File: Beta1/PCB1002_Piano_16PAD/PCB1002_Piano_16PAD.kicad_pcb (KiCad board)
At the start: 2 copper layers, 194 x 64 mm, 47 parts, among them U1 MPR121OTS, U2 MPR121OTS, U3 MPR121OTS

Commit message: Placement Done.
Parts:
- removed +3.3VA0, +3.3VB0, +3.3VC0, GNDA0, GNDB0, GNDC0, IRQA0, IRQB0, IRQC0, SCLA0, SCLB0, SCLC0, SDAA0, SDAB0, SDAC0: CONN_01X01, Liberry:single_0.1
- removed the REF** at (20.3, -2.54)
- removed the REF** at (8.64, -39.6)
- removed U2, U3: MPR121OTS, Liberry:MPR121OTS
- added A0: CONN_01X01, Liberry:TH_0.1_1x2_Jumper, F.Cu at (6.35, -22.9)
- added A1: CONN_01X01, Liberry:TH_0.1_1x2_Jumper, F.Cu at (6.35, -20.3)
- added A2: CONN_01X01, Liberry:TH_0.1_1x2_Jumper, F.Cu at (6.35, -17.8)
- added A3: CONN_01X01, Liberry:TH_0.1_1x2_Jumper, F.Cu at (6.35, -15.2)
- added A4: CONN_01X01, Liberry:TH_0.1_1x2_Jumper, F.Cu at (6.35, -12.7)
- added A5: CONN_01X01, Liberry:TH_0.1_1x2_Jumper, F.Cu at (6.35, -10.2)
- added C1: CC0603KRX7R9BB104, Capacitors_SMD:C_0603, B.Cu at (12.7, -50.8)
- added C101: CC0603KRX7R9BB104, Capacitors_SMD:C_0603, B.Cu at (12.7, -22.9)
- added C102: 0.1uf, Capacitors_SMD:C_0603, B.Cu at (12.7, -39.4)
- added C2: 0.1uf, Capacitors_SMD:C_0603, B.Cu at (12.7, -61.0)
- added C201: CC0603KRX7R9BB104, Capacitors_SMD:C_0603, B.Cu at (12.7, -3.29)
- added C202: 0.1uf, Capacitors_SMD:C_0603, B.Cu at (12.7, -15.2)
- added P0: CONN_01X01, Liberry:TESTPAD, B.Cu at (33.8, -52.1)
- added P1: CONN_01X01, Liberry:TESTPAD, B.Cu at (53.8, -52.1)
- added P10: CONN_01X01, Liberry:TESTPAD, B.Cu at (17.8, -48.3)
- added P100: CONN_01X01, Liberry:TESTPAD, B.Cu at (33.8, -32.1)
- added P101: CONN_01X01, Liberry:TESTPAD, B.Cu at (53.8, -32.1)
- added P102: CONN_01X01, Liberry:TESTPAD, B.Cu at (73.8, -32.1)
- added P103: CONN_01X01, Liberry:TESTPAD, B.Cu at (93.8, -32.1)
- added P104: CONN_01X01, Liberry:TESTPAD, B.Cu at (113.8, -32.1)
- added P105: CONN_01X01, Liberry:TESTPAD, B.Cu at (133.8, -32.1)
- added P106: CONN_01X01, Liberry:TESTPAD, B.Cu at (153.8, -32.1)
- added P107: CONN_01X01, Liberry:TESTPAD, B.Cu at (173.3, -32.1)
- added P108: CONN_01X01, Liberry:TESTPAD, B.Cu at (22.9, -22.9)
- added P109: CONN_01X01, Liberry:TESTPAD, B.Cu at (20.3, -22.9)
- added P11: CONN_01X01, Liberry:TESTPAD, B.Cu at (15.2, -48.3)
- added P110: CONN_01X01, Liberry:TESTPAD, B.Cu at (17.8, -22.9)
- added P111: CONN_01X01, Liberry:TESTPAD, B.Cu at (15.2, -22.9)
- added P2: CONN_01X01, Liberry:TESTPAD, B.Cu at (73.8, -52.1)
- added P200: CONN_01X01, Liberry:TESTPAD, B.Cu at (35.2, -4.88)
- added P201: CONN_01X01, Liberry:TESTPAD, B.Cu at (46.6, -16.1)
- added P202: CONN_01X01, Liberry:TESTPAD, B.Cu at (58.0, -4.88)
- added P203: CONN_01X01, Liberry:TESTPAD, B.Cu at (69.5, -16.1)
- added P204: CONN_01X01, Liberry:TESTPAD, B.Cu at (80.9, -4.88)
- added P205: CONN_01X01, Liberry:TESTPAD, B.Cu at (103.8, -4.88)
- added P206: CONN_01X01, Liberry:TESTPAD, B.Cu at (115.2, -16.1)
- added P207: CONN_01X01, Liberry:TESTPAD, B.Cu at (126.6, -4.88)
- added P208: CONN_01X01, Liberry:TESTPAD, B.Cu at (138.0, -16.1)
- added P209: CONN_01X01, Liberry:TESTPAD, B.Cu at (149.5, -4.88)
- added P210: CONN_01X01, Liberry:TESTPAD, B.Cu at (160.9, -16.1)
- added P211: CONN_01X01, Liberry:TESTPAD, B.Cu at (172.3, -4.88)
- added P3: CONN_01X01, Liberry:TESTPAD, B.Cu at (93.8, -52.1)
- added P4: CONN_01X01, Liberry:TESTPAD, B.Cu at (113.8, -52.1)
- added P5: CONN_01X01, Liberry:TESTPAD, B.Cu at (133.8, -52.1)
- added P6: CONN_01X01, Liberry:TESTPAD, B.Cu at (153.8, -52.1)
- added P7: CONN_01X01, Liberry:TESTPAD, B.Cu at (173.8, -52.1)
- added P8: CONN_01X01, Liberry:TESTPAD, B.Cu at (22.9, -48.3)
- added P9: CONN_01X01, Liberry:TESTPAD, B.Cu at (20.3, -48.3)
- added R1: 75K, Resistors_SMD:R_0603, B.Cu at (17.8, -61.0)
- added R101: 75K, Resistors_SMD:R_0603, B.Cu at (17.8, -39.4)
- added R102: 100K, Resistors_SMD:R_0603, B.Cu at (15.2, -39.4)
- added R2: 100K, Resistors_SMD:R_0603, B.Cu at (15.2, -61.0)
- added R201: 75K, Resistors_SMD:R_0603, B.Cu at (17.8, -15.2)
- added R202: 100K, Resistors_SMD:R_0603, B.Cu at (15.2, -15.2)
- added R301: 10K, Resistors_SMD:R_0603, B.Cu at (11.4, -33.0)
- added R302: 10K, Resistors_SMD:R_0603, B.Cu at (11.4, -30.5)
- added R303: 10K, Resistors_SMD:R_0603, B.Cu at (11.4, -35.6)
- added REF**: Fiducial_1mm_Dia_2.54mm_Outer_CopperBottom, Fiducials:Fiducial_1mm_Dia_2.54mm_Outer_CopperBottom, F.Cu at (7.62, -55.9)
- added U100: MPR121QR2, Liberry:QFN-20-1EP_3x3mm_Pitch0.40mm, B.Cu at (20.3, -29.3)
- added U200: MPR121QR2, Liberry:QFN-20-1EP_3x3mm_Pitch0.40mm, B.Cu at (20.3, -9.36)
- +3.3V0, GND0, IRQ0, SCL0, SDA0: footprint Liberry:single_0.1 -> Liberry:TH_0.1_1x2_Jumper
- U1: value MPR121OTS -> MPR121QR2; footprint Liberry:MPR121OTS -> Liberry:QFN-20-1EP_3x3mm_Pitch0.40mm; moved to B.Cu
- moved U1 24.2 mm to (20.3, -54.7)
- moved +3.3V0 20.4 mm to (6.35, -35.6)
- moved GND0 20.4 mm to (6.35, -25.4)
- moved IRQ0 20.4 mm to (6.35, -33.0)
- moved SCL0 20.4 mm to (6.35, -27.9)
- moved SDA0 20.4 mm to (6.35, -30.5)
- moved REF** 2.54 mm to (188.4, -3.00)
- moved REF** 2.54 mm to (5.54, -61.2)
- moved REF** 2.54 mm to (5.54, -3.00)
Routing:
- net (no net): track 190.0 -> 0.00 mm
- net Net-(P107-Pad1): track 183.6 -> 0.00 mm, vias 1 -> 0
- net Net-(P211-Pad1): track 178.9 -> 0.00 mm, vias 1 -> 0
- net /PAD7: track 167.6 -> 0.00 mm, vias 1 -> 0
- net Net-(P210-Pad1): track 160.6 -> 0.00 mm, vias 1 -> 0
- net Net-(P209-Pad1): track 154.7 -> 0.00 mm, vias 1 -> 0
- net Net-(P106-Pad1): track 152.8 -> 0.00 mm, vias 1 -> 0
- net /PAD6: track 147.2 -> 0.00 mm, vias 1 -> 0
- net Net-(P208-Pad1): track 140.0 -> 0.00 mm, vias 1 -> 0
- net Net-(P207-Pad1): track 129.0 -> 0.00 mm, vias 1 -> 0
- net Net-(P105-Pad1): track 127.7 -> 0.00 mm, vias 1 -> 0
- net /PAD5: track 122.9 -> 0.00 mm, vias 1 -> 0
- net Net-(P206-Pad1): track 115.2 -> 0.00 mm, vias 1 -> 0
- net Net-(P104-Pad1): track 107.7 -> 0.00 mm, vias 1 -> 0
- net Net-(P205-Pad1): track 106.6 -> 0.00 mm, vias 1 -> 0
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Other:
- board size 194 x 64 mm -> 188.9 x 64 mm
- board text added: "+3.3V"
- board text added: "0.1uF"
- board text added: "100K"
- board text added: "10K"
- board text added: "75K"
- board text added: "A0"
- board text added: "A1"
- board text added: "A2"
- board text added: "A3"
- board text added: "A4"
- board text added: "A5"
- board text added: "ADDR 0x5A (GND)"
- board text added: "ADDR 0x5B (+3.3V)"
- board text added: "ADDR 0x5C (SDA) (Yes, SDA)"
- board text added: "GND"
- board text added: "IRQ"
- board text added: "MPR121QR2 NRFND!"
- board text added: "PCB1002_Piano_16PAD_2017-01-26 Beta-1 Believotron Wanderlust 1/2 H Keypad 1 Octave Piano, 16 Pads"
- board text added: "SCL"
- board text added: "SDA"
- board text added: "x3"
- board text removed: "Once upon a time, there was a you, and you made the most beautiful frequencies. The darkness-at-the-end-of-the-universe quakes in agony at the beauty it will miss when your vibrations and their effects cease their joyful excitations."
- board text removed: "PCBBTKP Beta 1 - 2016-12-20 Believotron Wanderlust 1/2 H Keypad"

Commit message: Done routing.
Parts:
- added REF**: 1pin, Connect:1pin, F.Cu at (21.5, -3.00)
- added REF**: 1pin, Connect:1pin, F.Cu at (23.5, -61.2)
- moved P200 3.00 mm to (35.2, -7.88)
- moved P202 3.00 mm to (58.0, -7.88)
- moved P204 3.00 mm to (80.9, -7.88)
- moved P205 3.00 mm to (103.8, -7.88)
- moved P207 3.00 mm to (126.6, -7.88)
- moved P209 3.00 mm to (149.5, -7.88)
- moved P211 3.00 mm to (172.3, -7.88)
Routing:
- net Net-(P211-Pad1): track 0.00 -> 162.6 mm, vias 0 -> 1
- net /PAD7: track 0.00 -> 159.5 mm, vias 0 -> 1
- net Net-(P107-Pad1): track 0.00 -> 155.5 mm, vias 0 -> 1
- net Net-(P210-Pad1): track 0.00 -> 154.7 mm, vias 0 -> 1
- net /PAD6: track 0.00 -> 139.4 mm, vias 0 -> 1
- net Net-(P209-Pad1): track 0.00 -> 138.2 mm, vias 0 -> 1
- net Net-(P106-Pad1): track 0.00 -> 135.4 mm, vias 0 -> 1
- net Net-(P208-Pad1): track 0.00 -> 130.9 mm, vias 0 -> 1
- net GND: track 0.00 -> 129.9 mm, vias 0 -> 6
- net +3V3: track 0.00 -> 124.9 mm, vias 0 -> 10
- net /PAD5: track 0.00 -> 119.3 mm, vias 0 -> 1
- net Net-(P105-Pad1): track 0.00 -> 115.2 mm, vias 0 -> 1
- net Net-(P207-Pad1): track 0.00 -> 113.4 mm, vias 0 -> 1
- net /SCL: track 0.00 -> 108.7 mm
- net Net-(P206-Pad1): track 0.00 -> 108.3 mm, vias 0 -> 1
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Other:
- net class Default: clearance 0.2 -> 0.1524; trace_width 0.25 -> 0.1524
- rule trace_clearance: 0.2 -> 0.1524
- rule trace_min: 0.2 -> 0.1524
- rule via_min_drill: 0.3 -> 0.3302
- board text added: "MPR121QR2 QTYx3 NRFND!"
- board text added: "Open Source License at: https://github.com/Believotron/BelievotronWanderlustHardware Marketing pap: believotron.com The good stuff: http://community.believotron.com/"
- board text added: "PCB1002_Piano_16PAD_2017-01-26 Beta-1 Believotron Wanderlust 1/2 H Keypad 1 Octave Piano, 16 Pads 6CH Analog Mezzanine Expansion headers"
- board text removed: "MPR121QR2 NRFND!"
- board text removed: "PCB1002_Piano_16PAD_2017-01-26 Beta-1 Believotron Wanderlust 1/2 H Keypad 1 Octave Piano, 16 Pads"

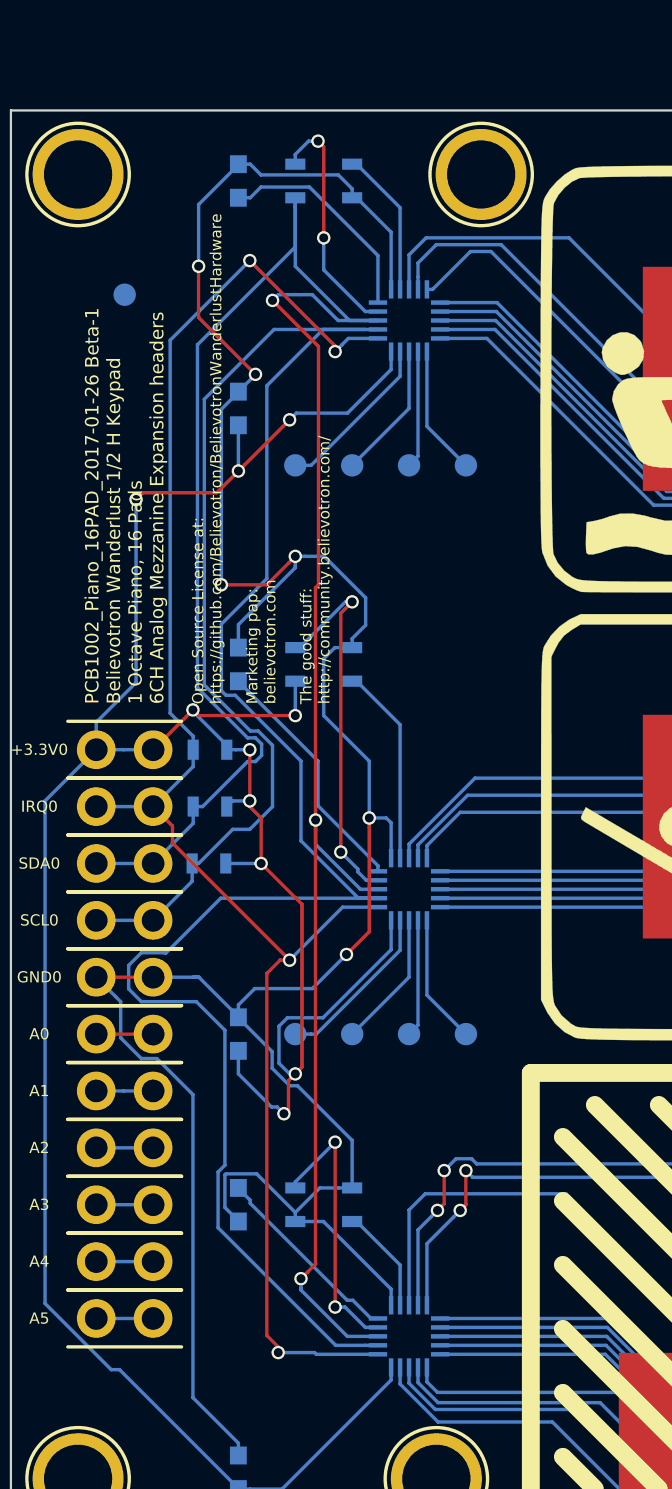
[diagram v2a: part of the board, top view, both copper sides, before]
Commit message: Added surplus padcap signal access to mezzanine
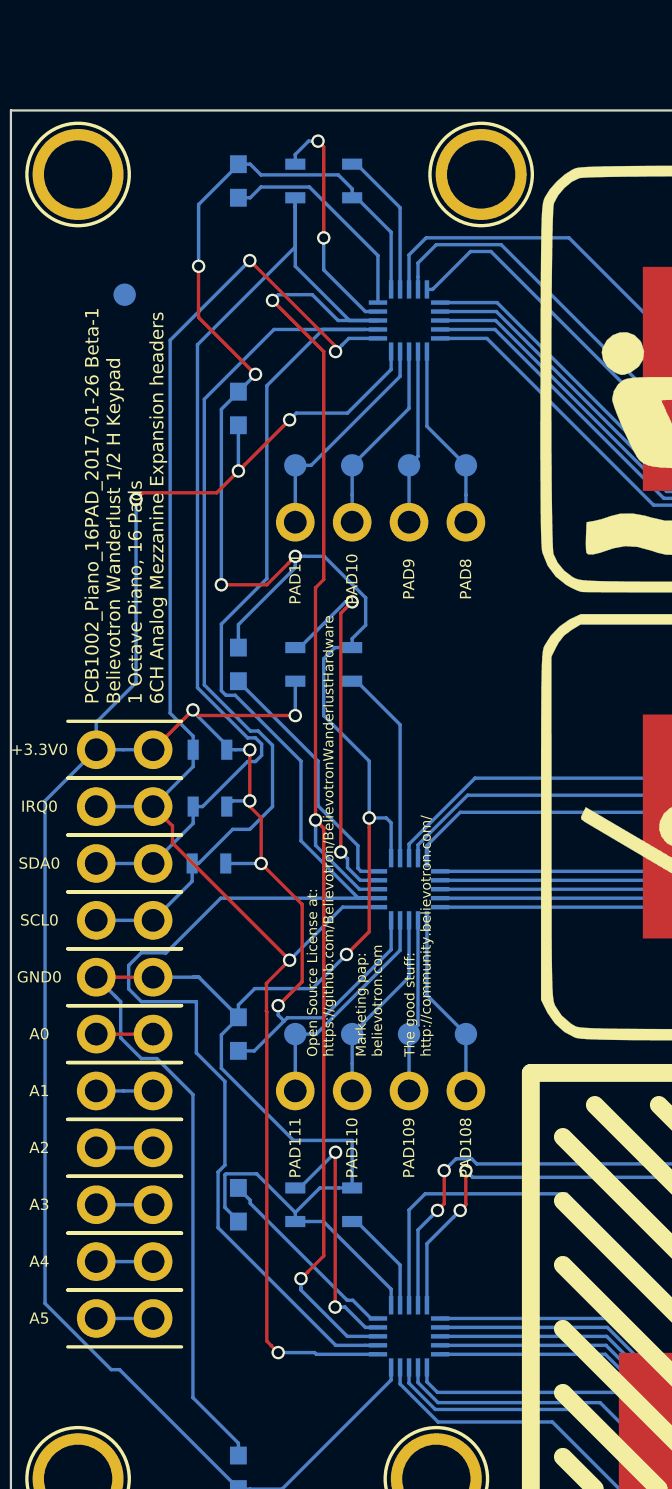
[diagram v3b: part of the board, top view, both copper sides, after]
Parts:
- added PAD10: CONN_01X01, Liberry:single_0.1, F.Cu at (17.8, -45.7)
- added PAD108: CONN_01X01, Liberry:single_0.1, F.Cu at (22.9, -20.3)
- added PAD109: CONN_01X01, Liberry:single_0.1, F.Cu at (20.3, -20.3)
- added PAD11: CONN_01X01, Liberry:single_0.1, F.Cu at (15.2, -45.7)
- added PAD110: CONN_01X01, Liberry:single_0.1, F.Cu at (17.8, -20.3)
- added PAD111: CONN_01X01, Liberry:single_0.1, F.Cu at (15.2, -20.3)
- added PAD8: CONN_01X01, Liberry:single_0.1, F.Cu at (22.9, -45.7)
- added PAD9: CONN_01X01, Liberry:single_0.1, F.Cu at (20.3, -45.7)
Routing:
- net +3V3: track 124.9 -> 116.8 mm, vias 10 -> 9
- net Net-(P111-Pad1): track 7.57 -> 10.1 mm
- net Net-(P9-Pad1): track 5.25 -> 7.79 mm
- net Net-(P8-Pad1): track 5.80 -> 8.34 mm
- net Net-(P110-Pad1): track 6.13 -> 8.67 mm
- net Net-(P11-Pad1): track 7.43 -> 9.97 mm
- net Net-(P109-Pad1): track 5.25 -> 7.79 mm
- net Net-(P108-Pad1): track 5.80 -> 8.34 mm
- net Net-(P10-Pad1): track 6.13 -> 8.67 mm
- net GND: track 129.9 -> 131.8 mm
- net Net-(R202-Pad2): track 12.4 -> 11.7 mm
- net /SDA: track 105.3 -> 105.9 mm
